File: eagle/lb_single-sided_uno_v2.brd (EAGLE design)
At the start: 68.6 x 53.3 mm, 16 parts, among them SW1 Button, SW3 Encoder

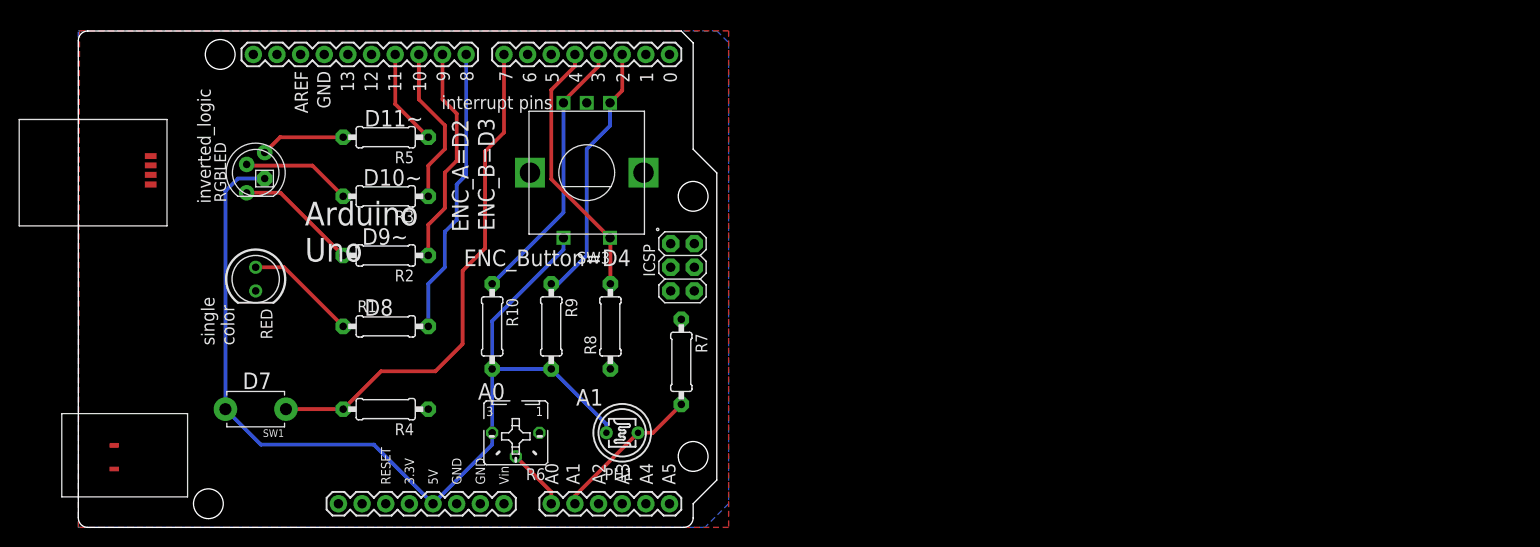
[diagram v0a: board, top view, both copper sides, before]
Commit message: needed to change the single sided board to SMD parts so they are solderable & provide practice
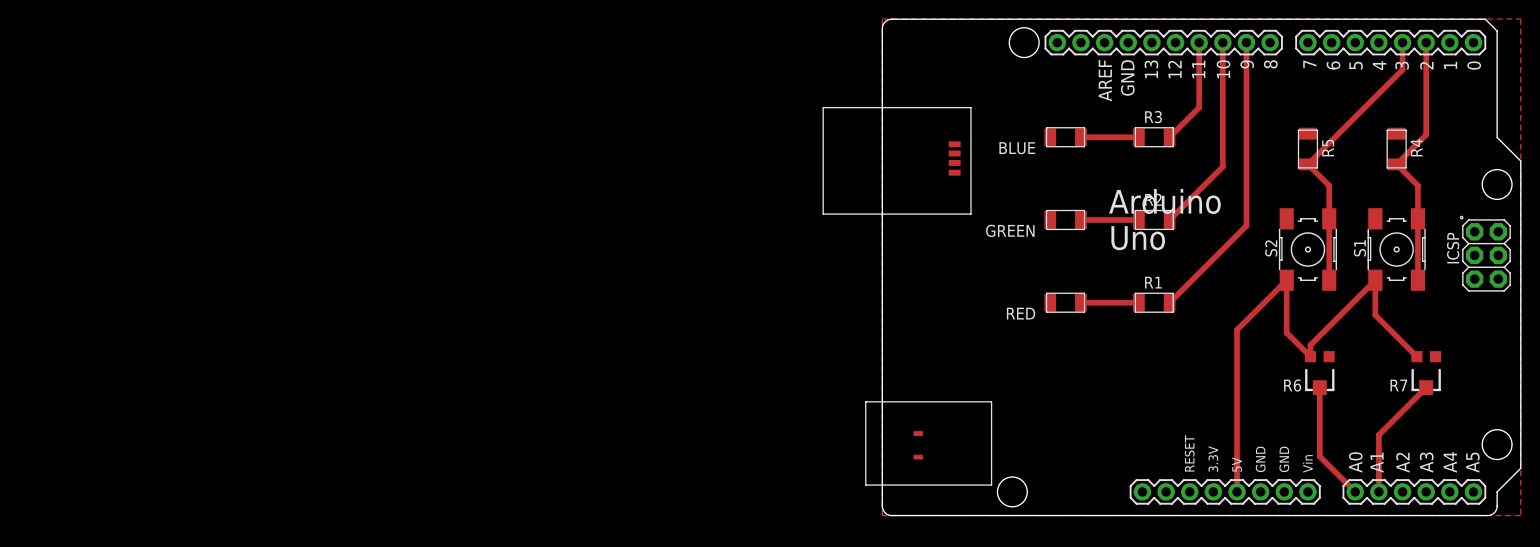
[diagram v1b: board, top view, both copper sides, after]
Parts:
- removed PH1: Light, photo-elements:T0-46-A10XX
- removed R10, R8, R9: 10k, adafruit:0207/9
- removed RGBLED: RGBLED, adafruit:LED5MMRGB
- removed SW1: Button, adafruit:TACT_PANA-EVQ
- removed SW3: Encoder, switch-alps:ALPS_EC12E_SW
- added BLUE, GREEN: LEDFAB1206, fab:LED1206FAB
- added S1, S2: (no value), fab:6MM_SWITCH
- R1, R2, R3, R4: device adafruit:0207/9 -> fab:R1206FAB
- R5: value 330 -> 10k; device adafruit:0207/9 -> fab:R1206FAB
- R6: value POT -> 10k; device pot:B25P -> adafruit:TC33X
- R7: device adafruit:0207/9 -> adafruit:TC33X
- RED: value LED -> LEDFAB1206; device fab:5MM -> fab:LED1206FAB
- moved R4 112.1 mm to (59.1, 41.9), turned to 270 degrees
- moved R5 99.1 mm to (49.5, 41.9), turned to 270 degrees
- moved RED 87.0 mm to (23.5, 25.4), turned to 180 degrees
- moved R6 86.6 mm to (50.8, 17.8)
- moved PCB1 86.4 mm to (3.81, 2.54)
- moved R3 82.8 mm to (33.0, 43.2), turned to 0 degrees
- moved R2 82.6 mm to (33.0, 34.3), turned to 0 degrees
- moved R1 82.6 mm to (33.0, 25.4)
- moved R7 80.0 mm to (62.2, 17.8), turned to 180 degrees
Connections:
- removed net D4: PCB1.4, R8.2, SW3.D
- removed net D7: PCB1.7, R4.2, SW1.P$1
- removed net D8: PCB1.8, R1.2
- removed net N$4: R5.2, RGBLED.4
- net 5V: now also R6.3, R7.3, S1.4, S2.4; no longer PH1.1, R10.2, R6.E, R9.2, RGBLED.2, SW1.P$2, SW3.E
- net A0: now also R6.2; no longer R6.S
- net A1: no longer PH1.2
- net D10: now also R2.2; no longer R3.1
- net D11: now also R3.2; no longer R5.1
- net D2: now also R4.2, S1.1, S1.2; no longer R9.1, SW3.A
- net D3: now also R5.2, S2.1, S2.2; no longer R10.1, SW3.B
- net D9: now also R1.2; no longer R2.1
- net GND: now also BLUE.2, GREEN.2, R5.1, R6.1, RED.2; no longer R6.A, R8.1, RED.OUT, SW3.C
- net N$1: now also RED.1; no longer RED.IN
- net N$2: now also GREEN.1, R2.1; no longer R2.2, RGBLED.1
- net N$3: now also BLUE.1, R3.1; no longer R3.2, RGBLED.3
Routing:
- net D7: track 54.8 -> 0.00 mm
- net 5V: track 104.7 -> 55.4 mm
- net D8: track 30.9 -> 0.00 mm
- net D4: track 28.3 -> 0.00 mm
- net D3: track 29.4 -> 41.4 mm
- net D2: track 28.2 -> 38.5 mm
- net N$4: track 9.11 -> 0.00 mm
- net D9: track 23.5 -> 31.4 mm
- net N$2: track 13.2 -> 6.22 mm
- net A0: track 6.66 -> 12.8 mm
- net N$1: track 12.0 -> 6.22 mm
- net N$3: track 11.8 -> 6.22 mm
- net D10: track 17.1 -> 21.4 mm
- net A1: track 16.3 -> 13.3 mm
- net D11: track 10.4 -> 11.5 mm
- removed copper zone on layer 16, net GND
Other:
- board text added: "LED"
- board text removed: "A0"
- board text removed: "A1"
- board text removed: "D10~"
- board text removed: "D11~"
- board text removed: "D7"
- board text removed: "D8"
- board text removed: "D9~"
- board text removed: "ENC_A=D2"
- board text removed: "ENC_B=D3"
- board text removed: "ENC_Button=D4"
- board text removed: "interrupt pins"
- board text removed: "inverted_logic"
- board text removed: "single color"

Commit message: updated board designs and docs
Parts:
- PCB1: value ARDUINO_UNO -> ARDUINO_UNO_V2; device E14_Arduino_revC:ARDUINO_UNO -> E14_Arduino_revC:ARDUINO_UNO_V2
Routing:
- net D2: track 38.5 -> 39.7 mm
- net D3: track 41.4 -> 42.2 mm
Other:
- outline, holes or cut-outs redrawn
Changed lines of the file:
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@@
 <board>
 <plain>
-<text x="20.955" y="45.085" size="2.54" layer="41" font="vector">LED</text>
-<text x="20.955" y="36.195" size="2.54" layer="41" font="vector">LED</text>
-<text x="20.955" y="27.305" size="2.54" layer="41" font="vector">LED</text>
+<text x="20.955" y="45.085" size="2.54" layer="41" font="vector" ratio="15">LED</text>
+<text x="20.955" y="36.195" size="2.54" layer="41" font="vector" ratio="15">LED</text>
+<text x="20.955" y="27.305" size="2.54" layer="41" font="vector" ratio="15">LED</text>
 </plain>
 <attributes>
@@
 <param name="srMinRoundness" value="0mil"/>
 <param name="srMaxRoundness" value="0mil"/>
-<param name="slThermalIsolate" value="10mil"/>
+<param name="slThermalIsolate" value="12mil"/>
 <param name="slThermalsForVias" value="0"/>
 <param name="dpMaxLengthDifference" value="10mm"/>
@@
 </autorouter>
 <elements>
-<element name="PCB1" library="E14_Arduino_revC" package="ARDUINO_UNO" value="ARDUINO_UNO" x="3.81" y="2.54" smashed="yes"/>
+<element name="PCB1" library="E14_Arduino_revC" package="ARDUINO_UNO_V2" value="ARDUINO_UNO_V2" x="3.81" y="2.54" smashed="yes"/>
 <element name="R1" library="fab" package="R1206FAB" value="330" x="33.02" y="25.4" smashed="yes">
 <attribute name="NAME" x="31.877" y="26.924" size="1.27" layer="25" ratio="10"/>
@@
 <wire x1="51.816" y1="34.417" x2="51.816" y2="37.973" width="0.6096" layer="1"/>
 <wire x1="51.816" y1="37.973" x2="49.53" y2="40.259" width="0.6096" layer="1"/>
-<wire x1="49.53" y1="40.259" x2="59.69" y2="50.419" width="0.6096" layer="1"/>
-<wire x1="59.69" y1="50.419" x2="59.69" y2="53.34" width="0.6096" layer="1"/>
+<wire x1="49.53" y1="40.259" x2="51.054" y2="40.259" width="0.6096" layer="1"/>
+<wire x1="51.054" y1="40.259" x2="53.975" y2="43.18" width="0.6096" layer="1"/>
+<wire x1="53.975" y1="43.18" x2="53.975" y2="44.45" width="0.6096" layer="1"/>
+<wire x1="53.975" y1="44.45" x2="59.69" y2="50.165" width="0.6096" layer="1"/>
+<wire x1="59.69" y1="50.165" x2="59.69" y2="53.34" width="0.6096" layer="1"/>
 </signal>
 <signal name="D2">
@@
 <wire x1="61.341" y1="34.417" x2="61.341" y2="37.973" width="0.6096" layer="1"/>
 <wire x1="61.341" y1="37.973" x2="59.055" y2="40.259" width="0.6096" layer="1"/>
-<wire x1="59.055" y1="40.259" x2="62.23" y2="43.434" width="0.6096" layer="1"/>
-<wire x1="62.23" y1="43.434" x2="62.23" y2="53.34" width="0.6096" layer="1"/>
+<wire x1="59.055" y1="40.259" x2="61.214" y2="40.259" width="0.6096" layer="1"/>
+<wire x1="61.214" y1="40.259" x2="62.23" y2="41.275" width="0.6096" layer="1"/>
+<wire x1="62.23" y1="41.275" x2="62.23" y2="53.34" width="0.6096" layer="1"/>
 </signal>
 <signal name="5V">
